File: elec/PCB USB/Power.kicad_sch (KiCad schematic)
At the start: 23 parts, among them Q1 AO3401A, U4 AP7361C-33E

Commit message: push schema
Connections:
- net VBUS_USB_5V renamed VBUS
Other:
- moved on the sheet: C19, C22, D1, R11, TP3, U4

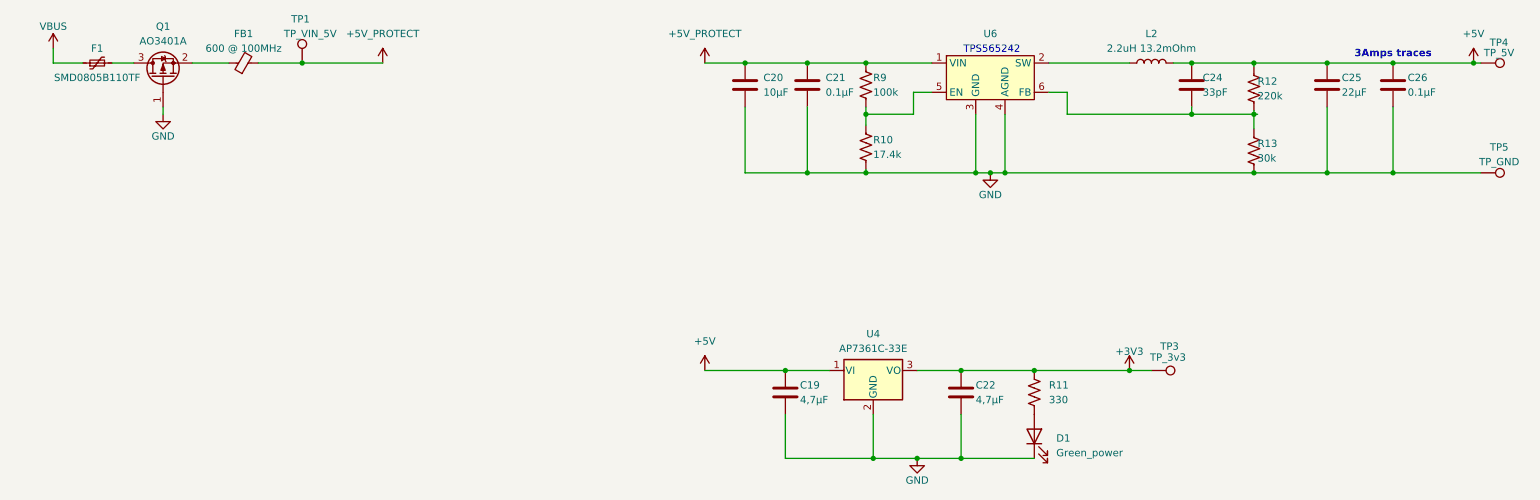
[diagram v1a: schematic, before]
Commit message: push sélection pièces et schéma électrique clean up
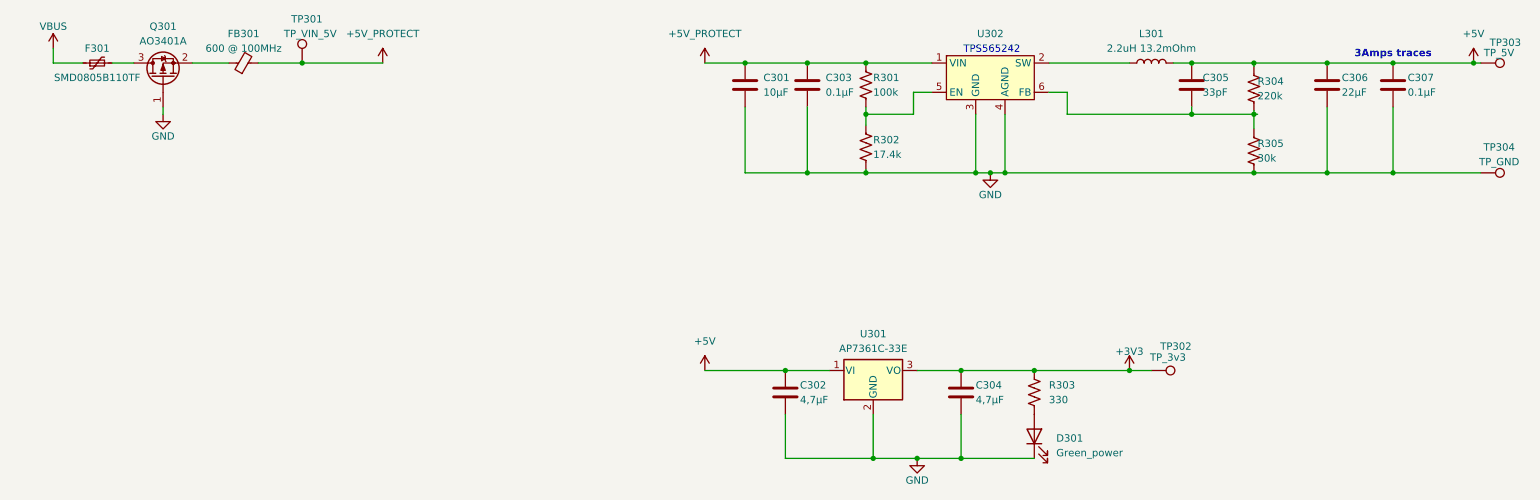
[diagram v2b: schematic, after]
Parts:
- renumbered C20 to C301, C19 to C302, C21 to C303, C22 to C304, C24 to C305, C25 to C306, C26 to C307, D1 to D301, F1 to F301, FB1 to FB301, L2 to L301, Q1 to Q301, R9 to R301, R10 to R302, R11 to R303, R12 to R304, R13 to R305, TP1 to TP301, TP3 to TP302, TP4 to TP303, TP5 to TP304, U4 to U301, U6 to U302

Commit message: push pcb
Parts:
- removed C301: 10µF, Capacitor_SMD:C_0805_2012Metric_Pad1.18x1.45mm_HandSolder, symbol Device:C
- removed C303, C307: 0.1µF, Capacitor_SMD:C_0603_1608Metric_Pad1.08x0.95mm_HandSolder, symbol Device:C
- removed C305: 33pF, Capacitor_SMD:C_0603_1608Metric_Pad1.08x0.95mm_HandSolder, symbol Device:C
- removed C306: 22µF, Capacitor_SMD:C_0805_2012Metric_Pad1.18x1.45mm_HandSolder, symbol Device:C
- removed L301: 2.2uH 13.2mOhm, Inductor_SMD:L_TDK_VLP8040, symbol Device:L
- removed R301: 100k, Resistor_SMD:R_0603_1608Metric_Pad0.98x0.95mm_HandSolder, symbol Device:R_US
- removed R302: 17.4k, Resistor_SMD:R_0603_1608Metric_Pad0.98x0.95mm_HandSolder, symbol Device:R_US
- removed R304: 220k, Resistor_SMD:R_0603_1608Metric_Pad0.98x0.95mm_HandSolder, symbol Device:R_US
- removed R305: 30k, Resistor_SMD:R_0603_1608Metric_Pad0.98x0.95mm_HandSolder, symbol Device:R_US
- removed TP303: TP_5V, TestPoint:TestPoint_Pad_D1.0mm, symbol Connector:TestPoint
- removed TP304: TP_GND, TestPoint:TestPoint_Pad_1.0x1.0mm, symbol Connector:TestPoint
- removed U302: ~, Package_TO_SOT_SMD:SOT-563, symbol TPS565242:TPS565242
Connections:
- net +5V_PROTECT is gone; now on net +5V: FB301.2, TP301.1
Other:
- note removed: "3Amps traces"
- note removed: "TPS565242"
- moved on the sheet: C302, C304, D301, R303, TP302, U301

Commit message: Push non terminé
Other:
- company: (none) -> C3I
- title: (none) -> Hub USB2.0 Pomodoro
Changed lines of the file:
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@@
 	(generator_version "9.0")
 	(paper "A4")
+	(title_block
+		(title "Hub USB2.0 Pomodoro")
+		(date "2025-04-20")
+		(rev "1.0")
+		(company "C3I")
+		(comment 1 "Jacob Turcotte")
+		(comment 2 "&")
+		(comment 3 "Charles-Ariel Dion")
+		(comment 4 "Par: Équipe 3")
+	)
 	(junction
 		(at 161.29 40.64)
